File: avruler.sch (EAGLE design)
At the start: 14 parts, among them IC1 TINY45, IC3 TINY45

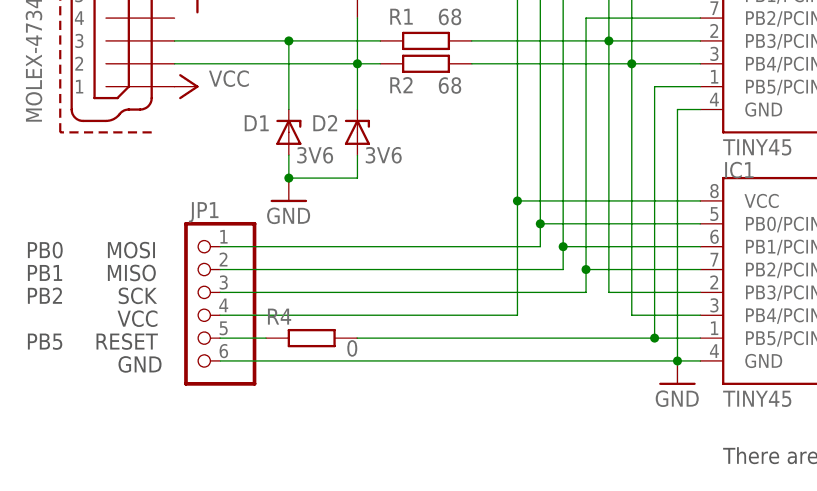
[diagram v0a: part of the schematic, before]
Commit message: swapped VCC and RESET on the pinheader
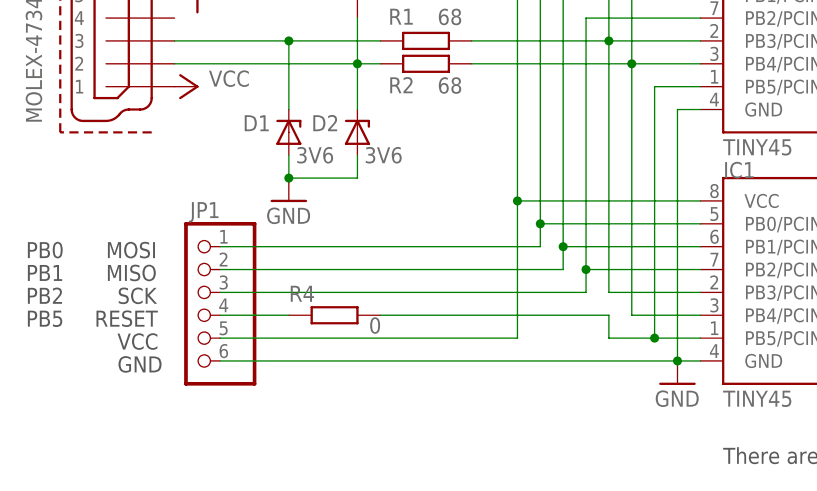
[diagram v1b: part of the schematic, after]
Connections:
- net N$10: now also JP1.4; no longer JP1.5
- net VCC: now also JP1.5; no longer JP1.4
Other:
- moved on the sheet: R4
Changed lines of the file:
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@@
 <text x="92.71" y="36.83" size="1.778" layer="97">There are two Tinys to cover both footprints (I get them wrong every single time...)</text>
 <text x="25.4" y="46.99" size="1.778" layer="97">GND</text>
-<text x="25.4" y="52.07" size="1.778" layer="97">VCC</text>
-<text x="22.86" y="49.53" size="1.778" layer="97">RESET</text>
+<text x="25.4" y="49.53" size="1.778" layer="97">VCC</text>
+<text x="22.86" y="52.07" size="1.778" layer="97">RESET</text>
 <text x="25.4" y="54.61" size="1.778" layer="97">SCK</text>
 <text x="24.13" y="57.15" size="1.778" layer="97">MISO</text>
@@
 <text x="15.24" y="57.15" size="1.778" layer="97">PB1</text>
 <text x="15.24" y="54.61" size="1.778" layer="97">PB2</text>
-<text x="15.24" y="49.53" size="1.778" layer="97">PB5</text>
+<text x="15.24" y="52.07" size="1.778" layer="97">PB5</text>
 <text x="81.28" y="107.95" size="1.778" layer="97" rot="R90">PB3</text>
 <text x="83.82" y="107.95" size="1.778" layer="97" rot="R90">PB4</text>
@@
 <attribute name="VALUE" x="40.64" y="43.18" size="1.778" layer="96" rot="MR0"/>
 </instance>
-<instance part="R4" gate="G$1" x="46.99" y="50.8" smashed="yes">
-<attribute name="NAME" x="41.91" y="52.2986" size="1.778" layer="95"/>
-<attribute name="VALUE" x="50.8" y="48.768" size="1.778" layer="96"/>
+<instance part="R4" gate="G$1" x="49.53" y="53.34" smashed="yes">
+<attribute name="NAME" x="44.45" y="54.8386" size="1.778" layer="95"/>
+<attribute name="VALUE" x="53.34" y="51.308" size="1.778" layer="96"/>
 </instance>
 <instance part="LED1" gate="G$1" x="49.53" y="111.76" smashed="yes" rot="R90">
@@
 <wire x1="85.09" y1="78.74" x2="90.17" y2="78.74" width="0.1524" layer="91"/>
 <pinref part="R4" gate="G$1" pin="2"/>
-<wire x1="52.07" y1="50.8" x2="85.09" y2="50.8" width="0.1524" layer="91"/>
+<wire x1="54.61" y1="53.34" x2="80.01" y2="53.34" width="0.1524" layer="91"/>
+<wire x1="80.01" y1="53.34" x2="80.01" y2="50.8" width="0.1524" layer="91"/>
+<wire x1="80.01" y1="50.8" x2="85.09" y2="50.8" width="0.1524" layer="91"/>
 <junction x="85.09" y="50.8"/>
 </segment>
@@
 <pinref part="P+2" gate="VCC" pin="VCC"/>
 <junction x="69.85" y="93.98"/>
-<wire x1="69.85" y1="53.34" x2="69.85" y2="66.04" width="0.1524" layer="91"/>
+<wire x1="69.85" y1="50.8" x2="69.85" y2="66.04" width="0.1524" layer="91"/>
 <junction x="69.85" y="66.04"/>
-<pinref part="JP1" gate="A" pin="4"/>
-<wire x1="36.83" y1="53.34" x2="69.85" y2="53.34" width="0.1524" layer="91"/>
+<pinref part="JP1" gate="A" pin="5"/>
+<wire x1="69.85" y1="50.8" x2="36.83" y2="50.8" width="0.1524" layer="91"/>
 </segment>
 <segment>
@@
 </segment>
 </net>
-<net name="N$10" class="0">
-<segment>
-<pinref part="R4" gate="G$1" pin="1"/>
-<pinref part="JP1" gate="A" pin="5"/>
-<wire x1="41.91" y1="50.8" x2="36.83" y2="50.8" width="0.1524" layer="91"/>
-</segment>
-</net>
 <net name="N$6" class="0">
 <segment>
@@
 </segment>
 </net>
+<net name="N$10" class="0">
+<segment>
+<pinref part="JP1" gate="A" pin="4"/>
+<pinref part="R4" gate="G$1" pin="1"/>
+<wire x1="36.83" y1="53.34" x2="44.45" y2="53.34" width="0.1524" layer="91"/>
+</segment>
+</net>
